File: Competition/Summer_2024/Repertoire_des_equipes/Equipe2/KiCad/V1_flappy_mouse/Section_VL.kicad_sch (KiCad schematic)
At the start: 20 parts, among them J301 ESP_GAUCHE, J302 ESP_DROIT, J304 Conn_TFT_display, U301 LM393

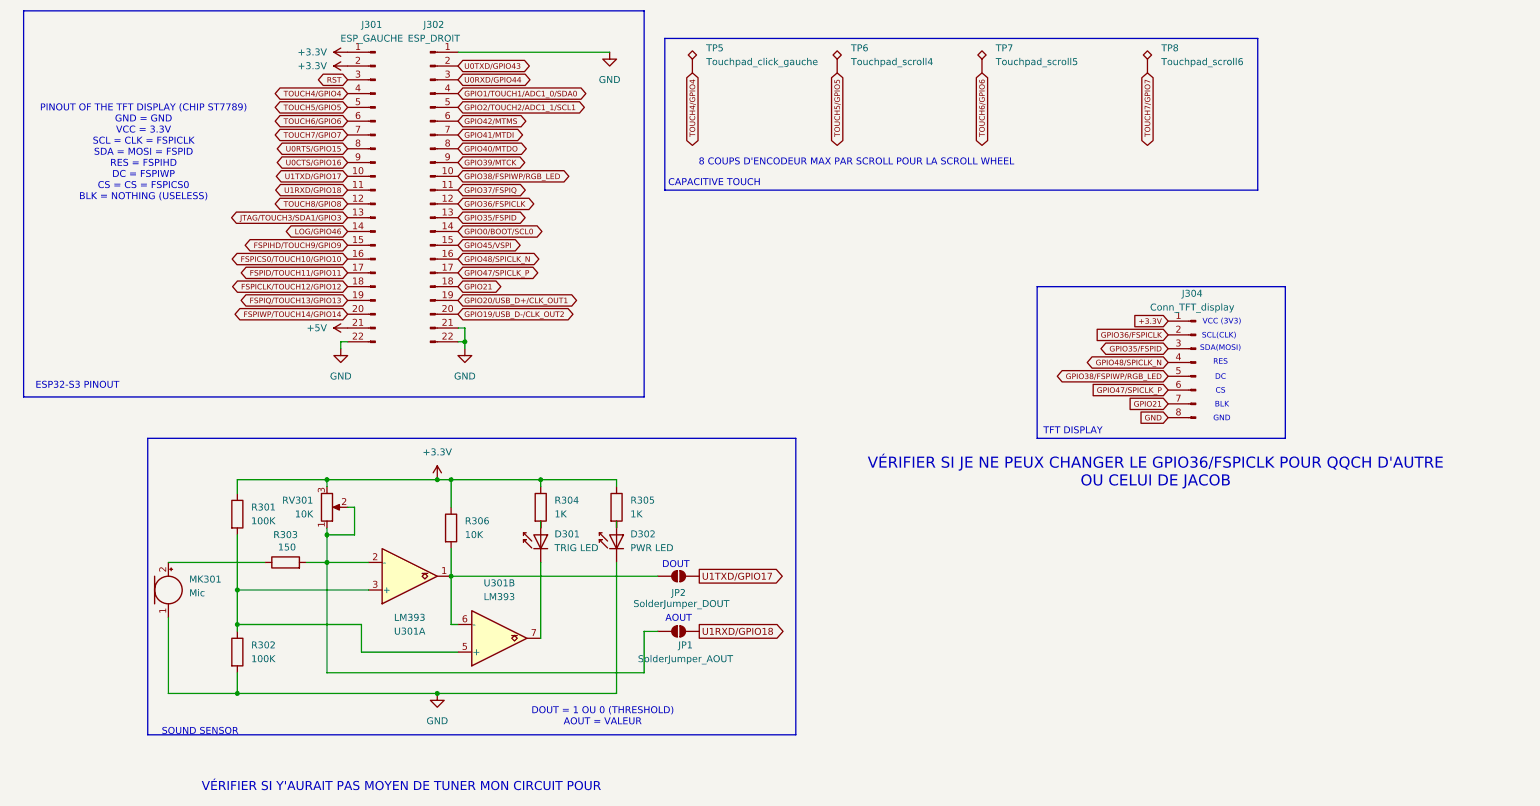
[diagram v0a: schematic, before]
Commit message: add the component on the PCB
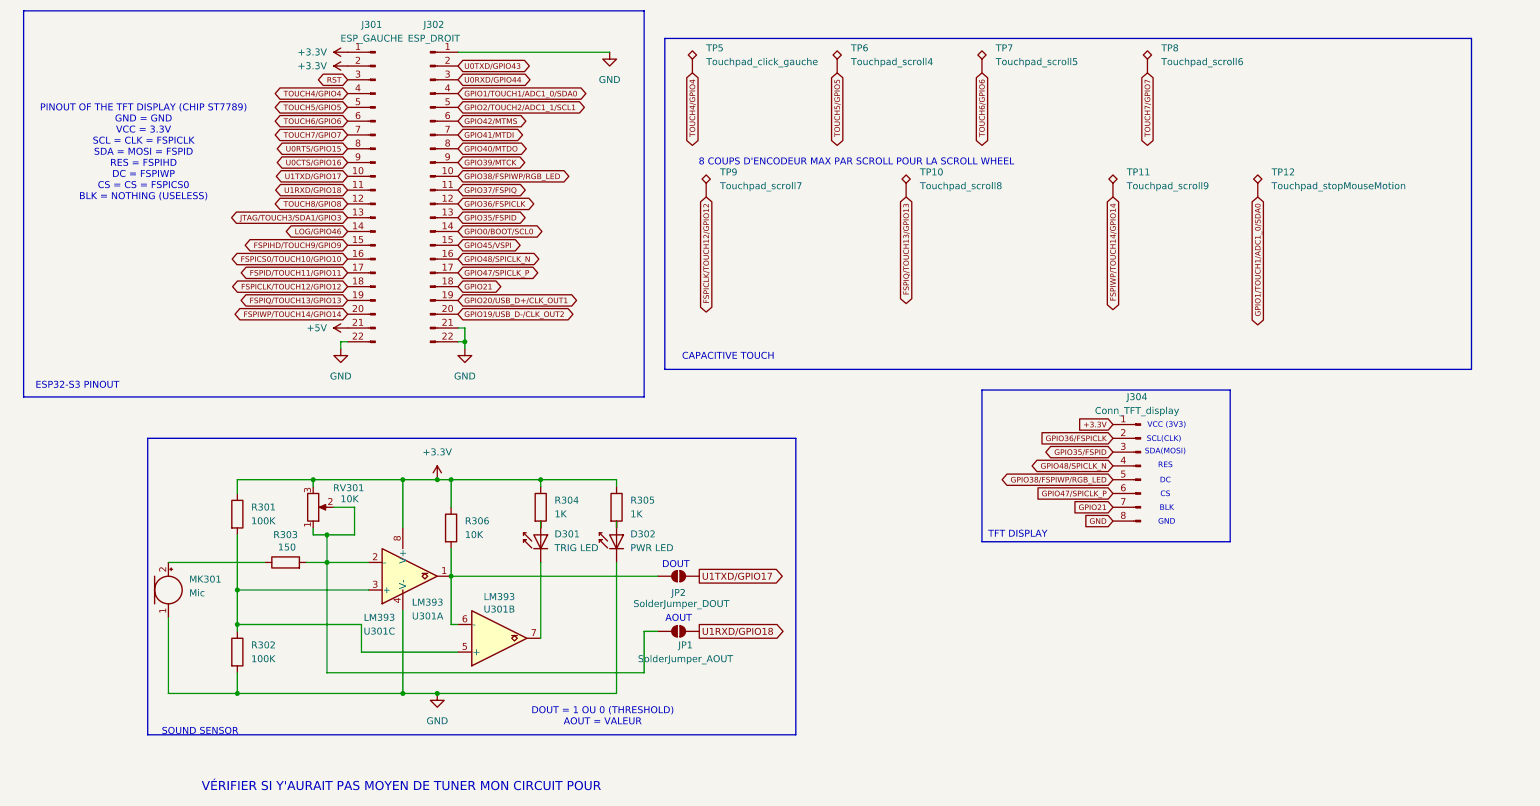
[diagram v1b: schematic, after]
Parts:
- added TP10: Touchpad_scroll8, Librairie_touchpad:Touchpad_slider_smaller, symbol Connector:TestPoint_Alt
- added TP11: Touchpad_scroll9, Librairie_touchpad:Touchpad_slider_smaller, symbol Connector:TestPoint_Alt
- added TP12: Touchpad_stopMouseMotion, Librairie_touchpad:Touchpad_biz_rect_smaller, symbol Connector:TestPoint_Alt
- added TP9: Touchpad_scroll7, Librairie_touchpad:Touchpad_slider_smaller, symbol Connector:TestPoint_Alt
- added unit 3 of U301
- JP1, JP2: footprint (none) -> Jumper:SolderJumper-2_P1.3mm_Open_RoundedPad1.0x1.5mm
- MK301: footprint (none) -> Buzzer_Beeper:Buzzer_12x9.5RM7.6
- R301, R302, R303, R304, R305, R306: footprint (none) -> Resistor_THT:R_Axial_DIN0207_L6.3mm_D2.5mm_P10.16mm_Horizontal
- RV301: footprint (none) -> Potentiometer_THT:Potentiometer_Piher_PT-10-V05_Vertical
- TP5: footprint Librairie_touchpad:Touchpad_biz_rect -> Librairie_touchpad:Touchpad_biz_rect_smaller
- TP6, TP7, TP8: footprint Librairie_touchpad:Touchpad_biz_rect -> Librairie_touchpad:Touchpad_slider_smaller
- U301: footprint (none) -> Package_DIP:CERDIP-8_W7.62mm_SideBrazed_Socket
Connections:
- net +3.3V: now also U301.8 (V+)
- net FSPICLK/TOUCH12/GPIO12: now also TP9.1
- net FSPIQ/TOUCH13/GPIO13: now also TP10.1
- net FSPIWP/TOUCH14/GPIO14: now also TP11.1
- net GND: now also U301.4 (V-)
- net GPIO1/TOUCH1/ADC1_0/SDA0: now also TP12.1
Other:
- note removed: "VÉRIFIER SI JE NE PEUX CHANGER LE GPIO36/FSPICLK POUR QQCH D'AUTRE OU CELUI DE JACOB"
- moved on the sheet: J304, RV301

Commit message: quick fix
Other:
- note removed: "PINOUT OF THE TFT DISPLAY (CHIP ST7789) GND = GND VCC = 3.3V SCL = CLK = FSPICLK SDA = MOSI = FSPID RES = FSPIHD DC = FSPIWP CS = CS = FSPICS0 BLK = NOTHING (USELESS)"
- moved on the sheet: RV301
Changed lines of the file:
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@@
+	)
+	(junction
+		(at 73.66 101.6)
+		(diameter 0)
+		(color 0 0 0 0)
 	)
 	(junction
@@
 	)
 	(junction
-		(at 71.12 101.6)
-		(diameter 0)
-		(color 0 0 0 0)
-	)
-	(junction
 		(at 73.66 111.76)
 		(diameter 0)
@@
 	(wire
 		(pts
-			(xy 71.12 101.6) (xy 87.63 101.6)
-		)
-		(stroke
-			(width 0)
-			(type default)
-		)
-	)
-	(wire
-		(pts
 			(xy 57.15 140.97) (xy 57.15 137.16)
 		)
@@
 	(wire
 		(pts
-			(xy 74.93 106.68) (xy 78.74 106.68)
+			(xy 77.47 106.68) (xy 78.74 106.68)
 		)
 		(stroke
@@
 	(wire
 		(pts
-			(xy 71.12 111.76) (xy 73.66 111.76)
-		)
-		(stroke
-			(width 0)
-			(type default)
-		)
-	)
-	(wire
-		(pts
-			(xy 57.15 101.6) (xy 71.12 101.6)
+			(xy 57.15 101.6) (xy 73.66 101.6)
 		)
 		(stroke
@@
 	(wire
 		(pts
-			(xy 71.12 102.87) (xy 71.12 101.6)
+			(xy 73.66 102.87) (xy 73.66 101.6)
 		)
 		(stroke
@@
 	(wire
 		(pts
+			(xy 73.66 101.6) (xy 87.63 101.6)
+		)
+		(stroke
+			(width 0)
+			(type default)
+		)
+	)
+	(wire
+		(pts
 			(xy 44.45 116.84) (xy 62.23 116.84)
 		)
@@
 	(wire
 		(pts
-			(xy 71.12 110.49) (xy 71.12 111.76)
+			(xy 73.66 110.49) (xy 73.66 111.76)
 		)
 		(stroke
@@
 			(font
 				(size 1.651 1.651)
-			)
-		)
-	)
-	(text "PINOUT OF THE TFT DISPLAY (CHIP ST7789)\nGND = GND\nVCC = 3.3V\nSCL = CLK = FSPICLK\nSDA = MOSI = FSPID\nRES = FSPIHD \nDC = FSPIWP\nCS = CS = FSPICS0\nBLK = NOTHING (USELESS)"
-		(exclude_from_sim no)
-		(at 39.878 41.402 0)
-		(effects
-			(font
-				(size 1.27 1.27)
 			)
 		)
@@
 	(symbol
 		(lib_id "Device:R_Potentiometer")
-		(at 71.12 106.68 0)
+		(at 73.66 106.68 0)
 		(mirror x)
 		(unit 1)
@@
 		(dnp no)
 		(property "Reference" "RV301"
-			(at 80.518 103.124 0)
+			(at 83.058 103.124 0)
 			(effects
 				(font
@@
 		)
 		(property "Value" "10K"
-			(at 79.502 105.156 0)
+			(at 82.042 105.156 0)
 			(effects
 				(font
@@
 		)
 		(property "Footprint" "Potentiometer_THT:Potentiometer_Piher_PT-10-V05_Vertical"
-			(at 71.12 106.68 0)
+			(at 73.66 106.68 0)
 			(effects
 				(font
@@
 		)
 		(property "Datasheet" "~"
-			(at 71.12 106.68 0)
+			(at 73.66 106.68 0)
 			(effects
 				(font
@@
 		)
 		(property "Description" "Potentiometer"
-			(at 71.12 106.68 0)
+			(at 73.66 106.68 0)
 			(effects
 				(font
@@
 					(reference "RV301")
 					(unit 1)
+				)
+			)
+			(project ""
+				(path "/c53b19f5-20eb-479e-abcd-b286f0e22d52"
+					(reference "RV301")
+					(unit 1)

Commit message: Push de PCB compléter à 80%
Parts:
- R301, R302, R303, R304, R305, R306: footprint Resistor_THT:R_Axial_DIN0207_L6.3mm_D2.5mm_P10.16mm_Horizontal -> Resistor_THT:R_Axial_DIN0207_L6.3mm_D2.5mm_P7.62mm_Horizontal
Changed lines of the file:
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@@
 		)
 		(instances
-			(project ""
+			(project "V1_flappy_mouse"
 				(path "/02a5dcc7-4b18-4a0b-b9f0-883e5dbce76c/f86b3f71-a906-482f-8366-32910134182f"
 					(reference "JP1")
@@
 			)
 		)
-		(property "Footprint" "Resistor_THT:R_Axial_DIN0207_L6.3mm_D2.5mm_P10.16mm_Horizontal"
+		(property "Footprint" "Resistor_THT:R_Axial_DIN0207_L6.3mm_D2.5mm_P7.62mm_Horizontal"
 			(at 94.742 110.49 90)
 			(effects
@@
 			)
 		)
-		(property "Footprint" "Resistor_THT:R_Axial_DIN0207_L6.3mm_D2.5mm_P10.16mm_Horizontal"
+		(property "Footprint" "Resistor_THT:R_Axial_DIN0207_L6.3mm_D2.5mm_P7.62mm_Horizontal"
 			(at 66.04 118.618 90)
 			(effects
@@
 			)
 		)
-		(property "Footprint" "Resistor_THT:R_Axial_DIN0207_L6.3mm_D2.5mm_P10.16mm_Horizontal"
+		(property "Footprint" "Resistor_THT:R_Axial_DIN0207_L6.3mm_D2.5mm_P7.62mm_Horizontal"
 			(at 125.222 106.68 90)
 			(effects
@@
 			)
 		)
-		(property "Footprint" "Resistor_THT:R_Axial_DIN0207_L6.3mm_D2.5mm_P10.16mm_Horizontal"
+		(property "Footprint" "Resistor_THT:R_Axial_DIN0207_L6.3mm_D2.5mm_P7.62mm_Horizontal"
 			(at 55.372 107.95 90)
 			(effects
@@
 			)
 		)
-		(property "Footprint" "Resistor_THT:R_Axial_DIN0207_L6.3mm_D2.5mm_P10.16mm_Horizontal"
+		(property "Footprint" "Resistor_THT:R_Axial_DIN0207_L6.3mm_D2.5mm_P7.62mm_Horizontal"
 			(at 111.252 106.68 90)
 			(effects
@@
 			)
 		)
-		(property "Footprint" "Resistor_THT:R_Axial_DIN0207_L6.3mm_D2.5mm_P10.16mm_Horizontal"
+		(property "Footprint" "Resistor_THT:R_Axial_DIN0207_L6.3mm_D2.5mm_P7.62mm_Horizontal"
 			(at 55.372 133.35 90)
 			(effects

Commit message: pcb 99% terminer
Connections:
- net +3.3V: now also J304.2 (Pin_2); no longer J304.1 (Pin_1)
- net GND: now also J304.1 (Pin_1); no longer J304.8 (Pin_8)
- net GPIO21: now also J304.8 (Pin_8); no longer J304.7 (Pin_7)
- net GPIO35/FSPID: now also J304.4 (Pin_4); no longer J304.3 (Pin_3)
- net GPIO36/FSPICLK: now also J304.3 (Pin_3); no longer J304.2 (Pin_2)
- net GPIO38/FSPIWP/RGB_LED: now also J304.6 (Pin_6); no longer J304.5 (Pin_5)
- net GPIO47/SPICLK_P: now also J304.7 (Pin_7); no longer J304.6 (Pin_6)
- net GPIO48/SPICLK_N: now also J304.5 (Pin_5); no longer J304.4 (Pin_4)
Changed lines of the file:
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@@
 	(wire
 		(pts
+			(xy 271.78 66.04) (xy 271.78 71.12)
+		)
+		(stroke
+			(width 0)
+			(type default)
+		)
+	)
+	(wire
+		(pts
 			(xy 96.52 128.27) (xy 97.79 128.27)
 		)
@@
 	(wire
 		(pts
+			(xy 217.17 99.06) (xy 218.44 99.06)
+		)
+		(stroke
+			(width 0)
+			(type default)
+		)
+	)
+	(wire
+		(pts
+			(xy 217.17 109.22) (xy 218.44 109.22)
+		)
+		(stroke
+			(width 0)
+			(type default)
+		)
+	)
+	(wire
+		(pts
 			(xy 113.03 116.84) (xy 113.03 130.81)
 		)
@@
 	(wire
 		(pts
+			(xy 217.17 106.68) (xy 218.44 106.68)
+		)
+		(stroke
+			(width 0)
+			(type default)
+		)
+	)
+	(wire
+		(pts
 			(xy 80.01 133.35) (xy 80.01 128.27)
 		)
@@
 	(wire
 		(pts
+			(xy 217.17 104.14) (xy 218.44 104.14)
+		)
+		(stroke
+			(width 0)
+			(type default)
+		)
+	)
+	(wire
+		(pts
 			(xy 93.98 101.6) (xy 96.52 101.6)
 		)
@@
 	(wire
 		(pts
+			(xy 217.17 93.98) (xy 218.44 93.98)
+		)
+		(stroke
+			(width 0)
+			(type default)
+		)
+	)
+	(wire
+		(pts
 			(xy 132.08 129.54) (xy 134.62 129.54)
 		)
@@
 	(wire
 		(pts
+			(xy 217.17 96.52) (xy 218.44 96.52)
+		)
+		(stroke
+			(width 0)
+			(type default)
+		)
+	)
+	(wire
+		(pts
 			(xy 78.74 106.68) (xy 78.74 111.76)
 		)
@@
 	(wire
 		(pts
+			(xy 217.17 101.6) (xy 218.44 101.6)
+		)
+		(stroke
+			(width 0)
+			(type default)
+		)
+	)
+	(wire
+		(pts
 			(xy 113.03 110.49) (xy 113.03 109.22)
 		)
@@
 	(wire
 		(pts
+			(xy 217.17 91.44) (xy 218.44 91.44)
+		)
+		(stroke
+			(width 0)
+			(type default)
+		)
+	)
+	(wire
+		(pts
 			(xy 73.66 110.49) (xy 73.66 111.76)
 		)
@@
 		)
 	)
-	(text "DC"
+	(text "RES"
 		(exclude_from_sim no)
-		(at 228.092 101.854 0)
+		(at 225.806 101.6 0)
 		(effects
 			(font
@@
 		)
 	)
-	(text "SDA(MOSI)\n"
+	(text "SCL(CLK)"
 		(exclude_from_sim no)
-		(at 228.092 96.52 0)
+		(at 224.028 96.774 0)
 		(effects
 			(font
 				(size 1.016 1.016)
 			)
+			(justify left)
 		)
 	)
-	(text "GND\n"
+	(text "BLK"
 		(exclude_from_sim no)
-		(at 228.346 109.474 0)
+		(at 226.06 109.474 0)
 		(effects
 			(font
@@
 		)
 	)
-	(text "VCC (3V3)\n\n"
+	(text "GND"
 		(exclude_from_sim no)
-		(at 228.346 92.456 0)
+		(at 224.028 91.694 0)
 		(effects
 			(font
 				(size 1.016 1.016)
 			)
+			(justify left)
 		)
 	)
@@
 		)
 	)
-	(text "BLK"
+	(text "CS"
 		(exclude_from_sim no)
-		(at 228.346 106.934 0)
+		(at 225.552 106.68 0)
 		(effects
 			(font
@@
 		)
 	)
-	(text "SCL(CLK)\n"
+	(text "VCC (3V3)"
 		(exclude_from_sim no)
-		(at 227.838 94.234 0)
+		(at 224.028 94.234 0)
 		(effects
 			(font
 				(size 1.016 1.016)
 			)
+			(justify left)
 		)
 	)
@@
 		)
 	)
-	(text "CS"
+	(text "DC"
 		(exclude_from_sim no)
-		(at 228.092 104.394 0)
+		(at 225.552 104.394 0)
 		(effects
 			(font
@@
 		)
 	)
-	(text "RES"
+	(text "SDA(MOSI)"
 		(exclude_from_sim no)
-		(at 228.092 99.06 0)
+		(at 224.028 99.314 0)
 		(effects
 			(font
 				(size 1.016 1.016)
 			)
+			(justify left)
 		)
 	)
@@
 	(global_label "GPIO47{slash}SPICLK_P"
 		(shape input)
-		(at 218.44 104.14 180)
+		(at 217.17 106.68 180)
 		(fields_autoplaced yes)
 		(effects
@@
 		)
 		(property "Intersheetrefs" "${INTERSHEET_REFS}"
-			(at 202.3603 104.14 0)
+			(at 201.0903 106.68 0)
 			(effects
 				(font
@@
 	(global_label "GPIO38{slash}FSPIWP{slash}RGB_LED"
 		(shape bidirectional)
-		(at 218.44 101.6 180)
+		(at 217.17 104.14 180)
 		(fields_autoplaced yes)
 		(effects
@@
 		)
 		(property "Intersheetrefs" "${INTERSHEET_REFS}"
-			(at 195.4237 101.6 0)
+			(at 194.1537 104.14 0)
 			(effects
 				(font
@@
 	(global_label "GPIO21"
 		(shape input)
-		(at 218.44 106.68 180)
+		(at 217.17 109.22 180)
 		(fields_autoplaced yes)
 		(effects
@@
 		)
 		(property "Intersheetrefs" "${INTERSHEET_REFS}"
-			(at 210.5367 106.68 0)
+			(at 209.2667 109.22 0)
 			(effects
 				(font
@@
 	(global_label "GPIO48{slash}SPICLK_N"
 		(shape bidirectional)
-		(at 218.44 99.06 180)
+		(at 217.17 101.6 180)
 		(fields_autoplaced yes)
 		(effects
@@
 		)
 		(property "Intersheetrefs" "${INTERSHEET_REFS}"
-			(at 201.4229 99.06 0)
+			(at 200.1529 101.6 0)
 			(effects
 				(font
@@
 	(global_label "GPIO35{slash}FSPID"
 		(shape bidirectional)
-		(at 218.44 96.52 180)
+		(at 217.17 99.06 180)
 		(fields_autoplaced yes)
 		(effects
@@
 		)
 		(property "Intersheetrefs" "${INTERSHEET_REFS}"
-			(at 204.229 96.52 0)
+			(at 202.959 99.06 0)
 			(effects
 				(font
@@
 	(global_label "+3.3V"
 		(shape input)
-		(at 218.44 91.44 180)
+		(at 217.17 93.98 180)
 		(fields_autoplaced yes)
 		(effects
@@
 		)
 		(property "Intersheetrefs" "${INTERSHEET_REFS}"
-			(at 211.5043 91.44 0)
+			(at 210.2343 93.98 0)
 			(effects
 				(font
@@
 	(global_label "GND"
 		(shape input)
-		(at 218.44 109.22 180)
+		(at 217.17 91.44 180)
 		(fields_autoplaced yes)
 		(effects
@@
 		)
 		(property "Intersheetrefs" "${INTERSHEET_REFS}"
-			(at 212.9557 109.22 0)
+			(at 211.6857 91.44 0)
 			(effects
 				(font
@@
 	(global_label "GPIO36{slash}FSPICLK"
 		(shape input)
-		(at 218.44 93.98 180)
+		(at 217.17 96.52 180)
 		(fields_autoplaced yes)
 		(effects
@@
 		)
 		(property "Intersheetrefs" "${INTERSHEET_REFS}"
-			(at 203.2795 93.98 0)
+			(at 202.0095 96.52 0)
 			(effects
 				(font
@@
 		)
 	)
+	(netclass_flag ""
+		(length 2.54)
+		(shape round)
+		(at 271.78 66.04 0)
+		(fields_autoplaced yes)
+		(effects
+			(font
+				(size 1.27 1.27)
+			)
+			(justify left bottom)
+		)
+		(property "Netclass" "SHIELD"
+			(at 272.4785 63.5 0)
+			(effects
+				(font
+					(size 1.27 1.27)
+					(italic yes)
+				)
+				(justify left)
+			)
+		)
+	)
 	(symbol
 		(lib_id "power:GND")
@@
 					(unit 1)
 				)
+			)
+		)
+	)
+	(symbol
+		(lib_id "power:GND1")
+		(at 271.78 71.12 0)
+		(unit 1)
+		(exclude_from_sim no)
+		(in_bom yes)
+		(on_board yes)
+		(dnp no)
+		(property "Reference" "#PWR0309"
+			(at 271.78 77.47 0)
+			(effects
+				(font
+					(size 1.27 1.27)
+				)
+				(hide yes)
+			)
+		)
+		(property "Value" "SHIELD"
+			(at 271.78 74.676 0)
+			(effects
+				(font
+					(size 1.27 1.27)
+				)
+			)
+		)
+		(property "Footprint" ""
+			(at 271.78 71.12 0)
+			(effects
+				(font
+					(size 1.27 1.27)
+				)
+				(hide yes)
+			)
+		)
+		(property "Datasheet" ""
+			(at 271.78 71.12 0)
+			(effects
+				(font
+					(size 1.27 1.27)
+				)
+				(hide yes)
+			)
+		)
+		(property "Description" "Power symbol creates a global label with name \"GND1\" , ground"
+			(at 271.78 71.12 0)
+			(effects
+				(font
+					(size 1.27 1.27)
+				)
+				(hide yes)
+			)
+		)
+		(pin "1"
+		)
+		(instances
+			(project "V1_flappy_mouse"
+				(path "/02a5dcc7-4b18-4a0b-b9f0-883e5dbce76c/f86b3f71-a906-482f-8366-32910134182f"
+					(reference "#PWR0309")
+					(unit 1)
+				)
